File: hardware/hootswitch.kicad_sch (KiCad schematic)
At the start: 66 parts, among them J1 Mini-DIN-4-G, J10 POWSEL, J11 TWI, J12 TWI, J2 Mini-DIN-4-G, J7 Barrel_Jack_MountingPin, J8 EXT_POW, J9 SW1, Q1 MMBT3904, Q2 MMBT3904, Q3 MMBT3904, Q4 MMBT3904, Q5 MMBT3904, Q6 MMBT3904, Q7 MMBT3904, Q8 MMBT3904, SW1 Switch1, U1 Pico, U2 LM1117-5.0, U7 ADuM1201AR

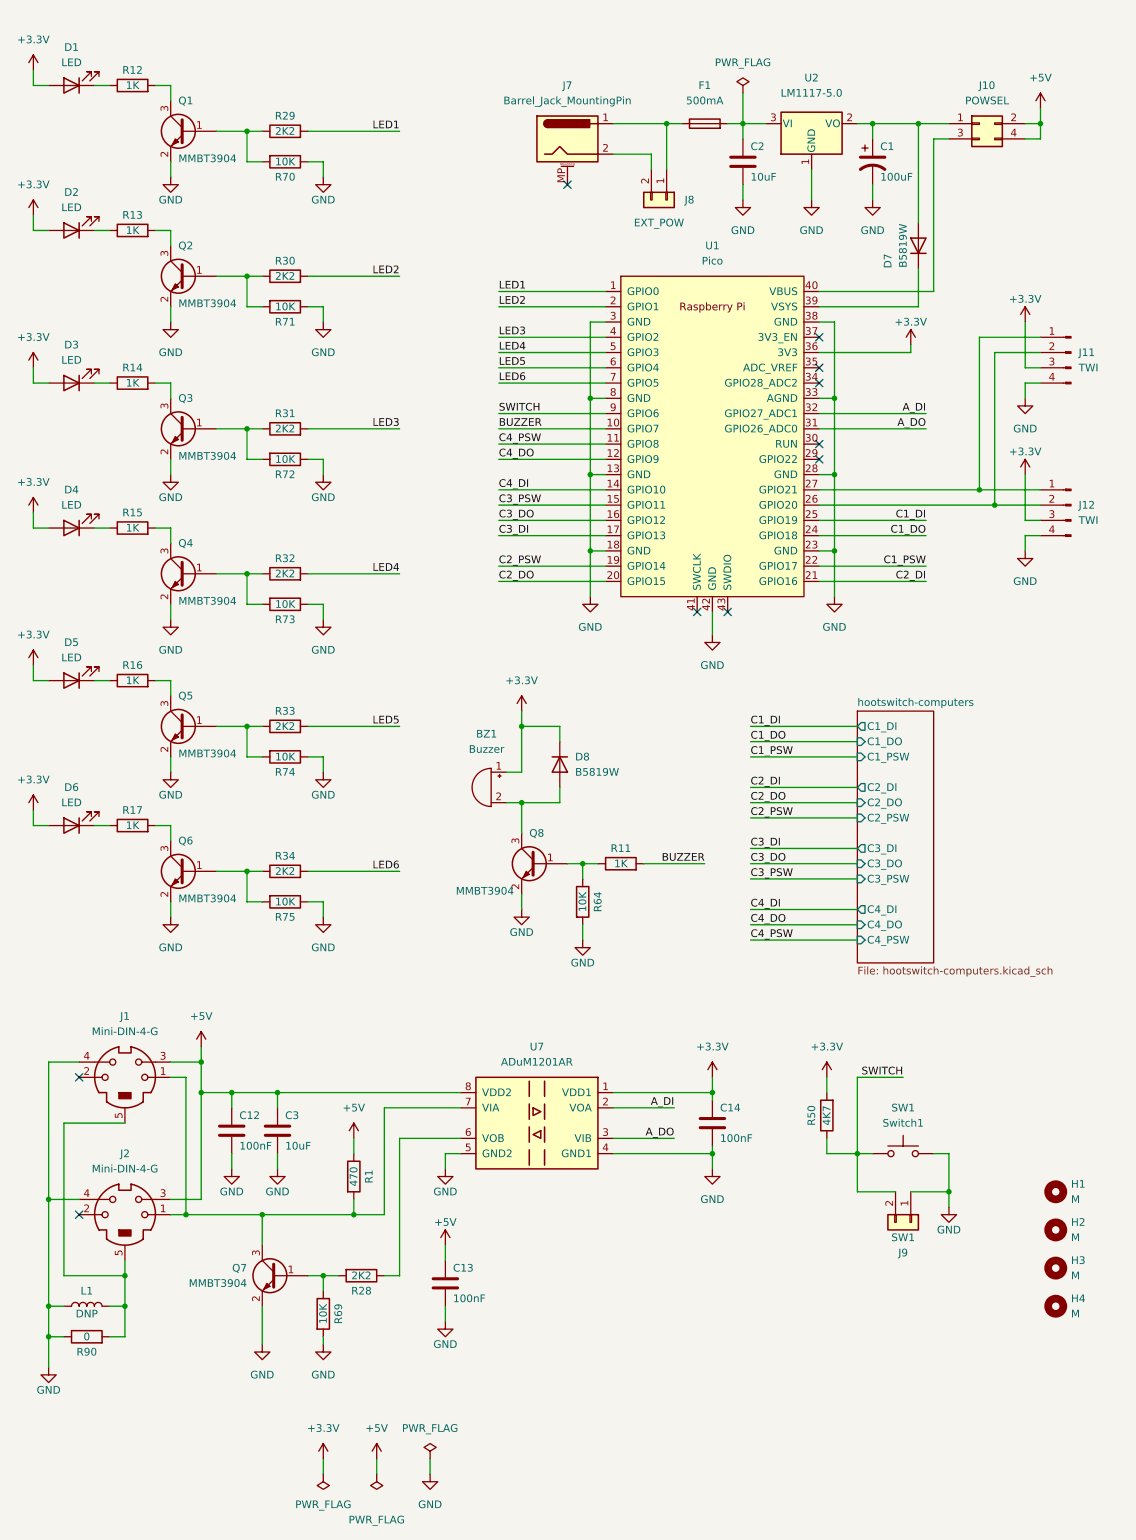
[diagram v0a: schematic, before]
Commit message: Hardware Fork: Use Mosfets For Isolation
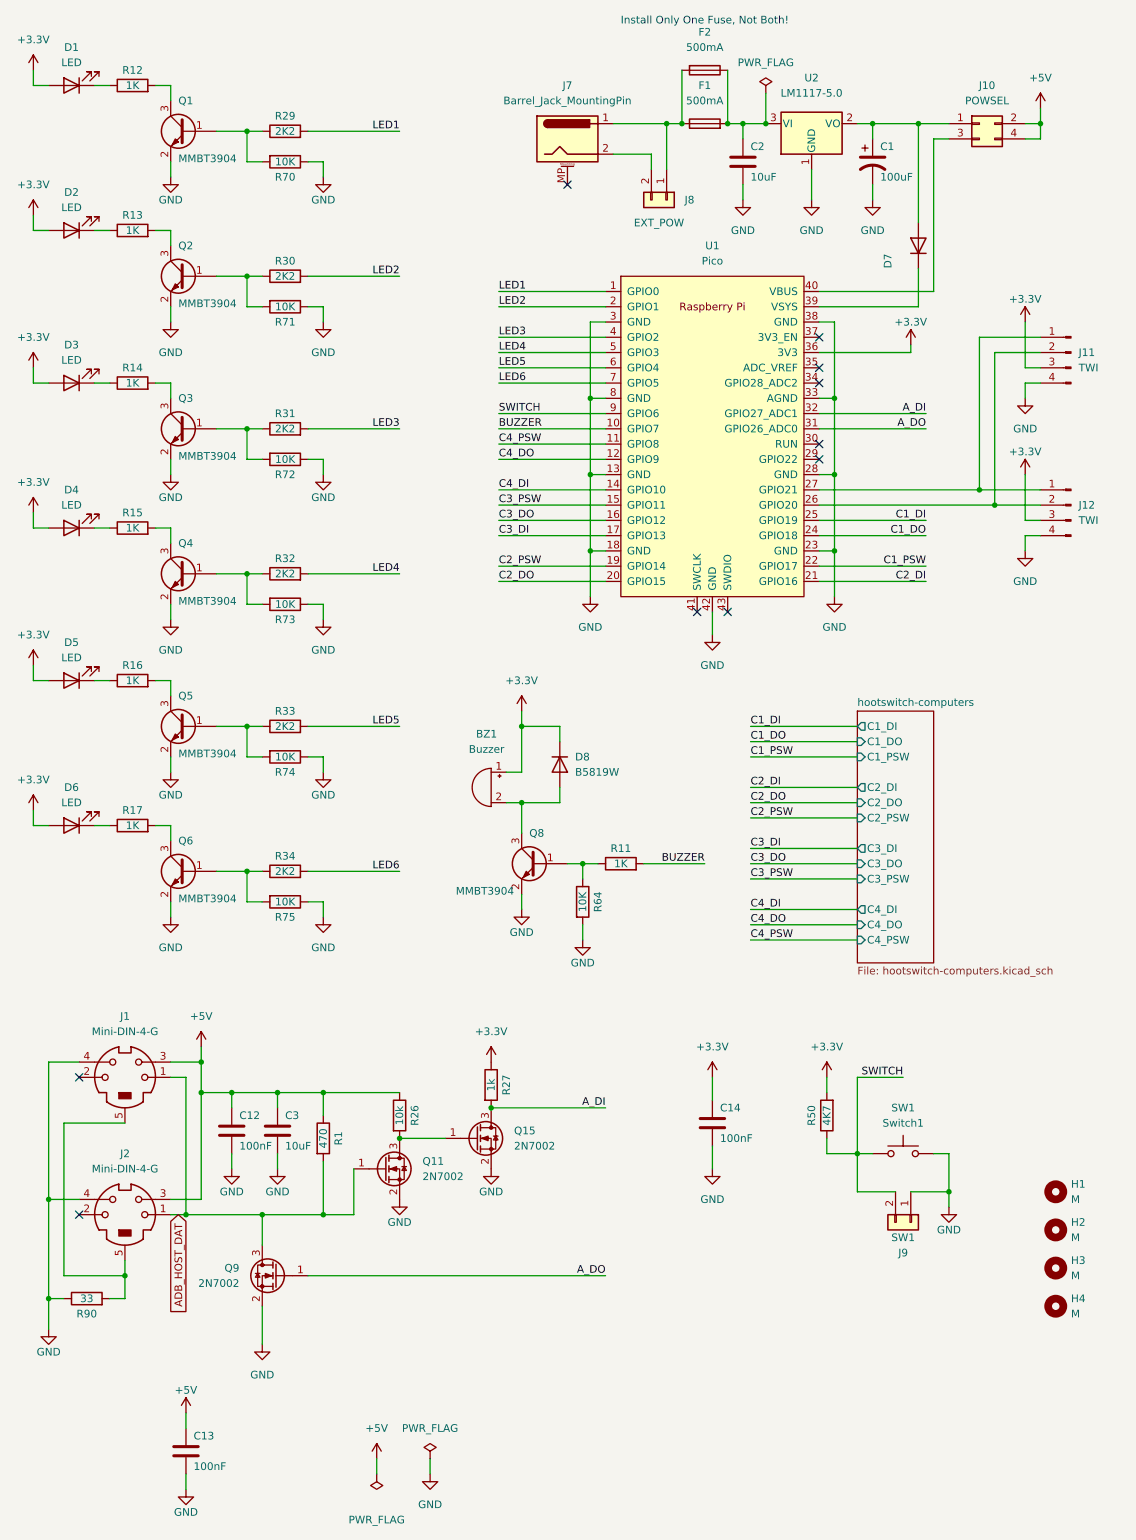
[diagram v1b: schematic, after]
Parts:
- removed L1: DNP, Inductor_SMD:L_0603_1608Metric, symbol Device:L
- removed Q7: MMBT3904, Package_TO_SOT_SMD:SOT-23, symbol Transistor_BJT:MMBT3904
- removed R28: 2K2, Resistor_SMD:R_0603_1608Metric, symbol Device:R
- removed R69: 10K, Resistor_SMD:R_0603_1608Metric, symbol Device:R
- removed U7: ADuM1201AR, Package_SO:SOIC-8_3.9x4.9mm_P1.27mm, symbol Isolator:ADuM1201AR
- added F2: 500mA, Fuse:Fuse_0805_2012Metric, symbol Device:Fuse
- added Q11, Q15, Q9: 2N7002, Package_TO_SOT_SMD:SOT-23, symbol Transistor_FET:2N7002
- added R26: 10k, Resistor_SMD:R_0603_1608Metric, symbol Device:R
- added R27: 1k, Resistor_SMD:R_0603_1608Metric, symbol Device:R
- D7: value B5819W -> ${SIM.PARAMS}; Spice_Netlist_Enabled Y -> (none); Spice_Primitive D -> (none)
- R90: value 0 -> 33
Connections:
- net +3.3V: now also R27.1
- net +5V: now also R26.1
- net A_DI: now also Q15.3 (D), R27.2
- net A_DO: now also Q9.1 (G)
- net GND: now also Q11.2 (S), Q15.2 (S), Q9.2 (S)
- net at C2.1, F1.2, U2.3 (VI): now also F2.1
- net ADB_HOST_DAT: now reaches J1.1, J2.1, R1.2
- net ADB_HOST_DAT: now also Q11.1 (G), Q9.3 (D)
- net at F1.1, J7.1, J8.1 (Pin_1): now also F2.2
- new net: Q11.3 (D), Q15.1 (G), R26.2
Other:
- note added: "Install Only One Fuse, Not Both!"
- moved on the sheet: C13, R1, R90
